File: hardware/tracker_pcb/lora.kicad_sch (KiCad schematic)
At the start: 3 parts, among them IC4 WIO-SX1262

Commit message: WIP
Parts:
- IC4: footprint 114993390 -> footprint:114993390
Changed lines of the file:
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@@
 			)
 		)
-		(property "Footprint" "114993390"
+		(property "Footprint" "footprint:114993390"
 			(at 139.7 166.04 0)
 			(effects

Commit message: Beef up 5v supply and add new power mux
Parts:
- renumbered C25 to C26, C24 to C27, IC4 to U12
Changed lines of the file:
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@@
 		(on_board yes)
 		(dnp no)
-		(property "Reference" "C24"
+		(property "Reference" "C27"
 			(at 92.202 92.964 0)
 			(effects
@@
 			(project "tracker_pcb"
 				(path "/6aaa9514-f94e-4843-90d0-16960e4e49cb/4b60d742-f193-431b-a1a9-b431b44dc8b4"
-					(reference "C24")
+					(reference "C27")
 					(unit 1)
 				)
@@
 		(on_board yes)
 		(dnp yes)
-		(property "Reference" "C25"
+		(property "Reference" "C26"
 			(at 78.232 92.964 0)
 			(effects
@@
 			(project "tracker_pcb"
 				(path "/6aaa9514-f94e-4843-90d0-16960e4e49cb/4b60d742-f193-431b-a1a9-b431b44dc8b4"
-					(reference "C25")
+					(reference "C26")
 					(unit 1)
 				)
@@
 		(dnp no)
 		(fields_autoplaced yes)
-		(property "Reference" "#PWR022"
+		(property "Reference" "#PWR026"
 			(at 127 105.41 0)
 			(effects
@@
 			(project ""
 				(path "/6aaa9514-f94e-4843-90d0-16960e4e49cb/4b60d742-f193-431b-a1a9-b431b44dc8b4"
-					(reference "#PWR022")
+					(reference "#PWR026")
 					(unit 1)
 				)
@@
 		(dnp yes)
 		(fields_autoplaced yes)
-		(property "Reference" "IC4"
+		(property "Reference" "U12"
 			(at 127 63.5 0)
 			(effects
@@
 			(project ""
 				(path "/6aaa9514-f94e-4843-90d0-16960e4e49cb/4b60d742-f193-431b-a1a9-b431b44dc8b4"
-					(reference "IC4")
+					(reference "U12")
 					(unit 1)
 				)

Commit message: Modify iso circuit for best CTR
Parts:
- renumbered C26 to C25, C27 to C26
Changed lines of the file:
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@@
 		(on_board yes)
 		(dnp no)
-		(property "Reference" "C27"
+		(property "Reference" "C26"
 			(at 92.202 92.964 0)
 			(effects
@@
 			(project "tracker_pcb"
 				(path "/6aaa9514-f94e-4843-90d0-16960e4e49cb/4b60d742-f193-431b-a1a9-b431b44dc8b4"
-					(reference "C27")
+					(reference "C26")
 					(unit 1)
 				)
@@
 		(on_board yes)
 		(dnp yes)
-		(property "Reference" "C26"
+		(property "Reference" "C25"
 			(at 78.232 92.964 0)
 			(effects
@@
 			(project "tracker_pcb"
 				(path "/6aaa9514-f94e-4843-90d0-16960e4e49cb/4b60d742-f193-431b-a1a9-b431b44dc8b4"
-					(reference "C26")
+					(reference "C25")
 					(unit 1)
 				)

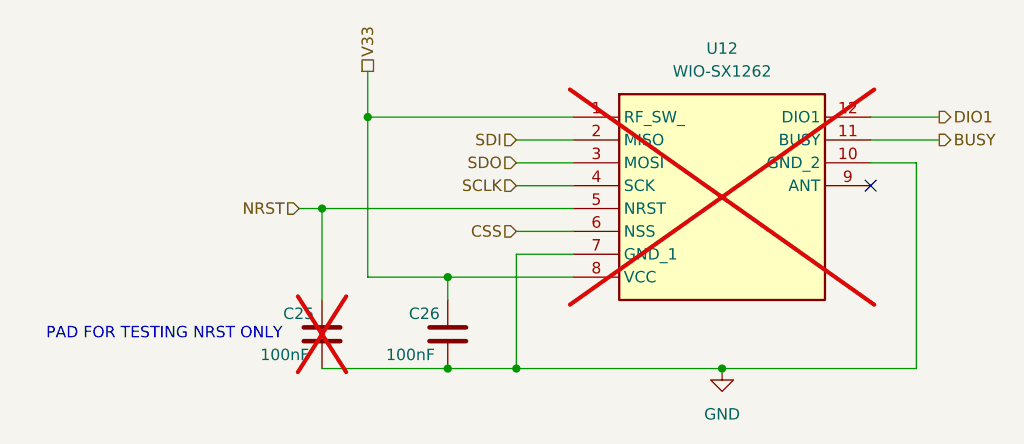
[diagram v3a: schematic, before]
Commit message: add 3pin jst for analog
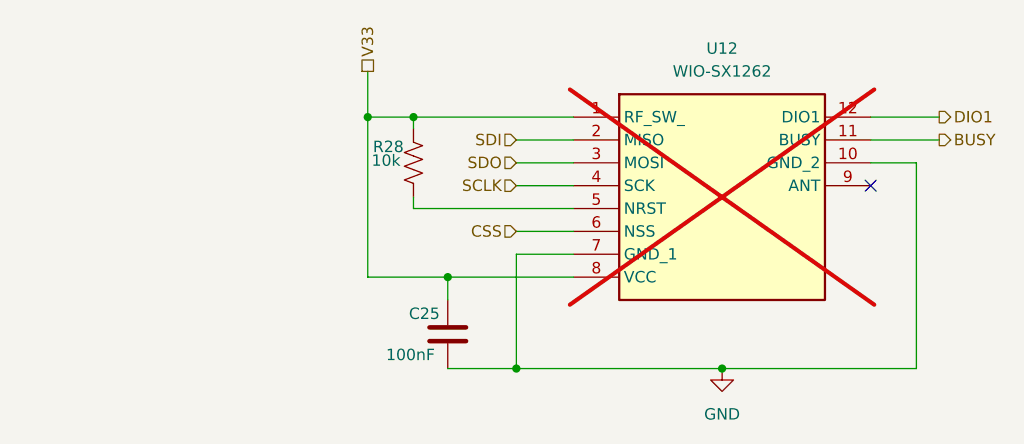
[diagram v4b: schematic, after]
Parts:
- removed C25: 100nF, Capacitor_SMD:C_0603_1608Metric, symbol Device:C
- added R28: 10k, Resistor_SMD:R_0805_2012Metric, symbol Device:R_US
- renumbered C26 to C25
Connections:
- net V33: now also R28.1
- net NRST: no longer names the net of U12.5 (NRST)
- net NRST: now also R28.2
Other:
- note removed: "PAD FOR TESTING NRST ONLY"

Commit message: v2 hardware changes
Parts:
- renumbered C25 to C27, R28 to R32, U12 to U13
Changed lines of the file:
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@@
 		(on_board yes)
 		(dnp no)
-		(property "Reference" "R28"
+		(property "Reference" "R32"
 			(at 89.916 74.422 0)
 			(effects
@@
 			(project "tracker_pcb"
 				(path "/6aaa9514-f94e-4843-90d0-16960e4e49cb/4b60d742-f193-431b-a1a9-b431b44dc8b4"
-					(reference "R28")
+					(reference "R32")
 					(unit 1)
 				)
@@
 		(on_board yes)
 		(dnp no)
-		(property "Reference" "C25"
+		(property "Reference" "C27"
 			(at 92.202 92.964 0)
 			(effects
@@
 			(project "tracker_pcb"
 				(path "/6aaa9514-f94e-4843-90d0-16960e4e49cb/4b60d742-f193-431b-a1a9-b431b44dc8b4"
-					(reference "C25")
+					(reference "C27")
 					(unit 1)
 				)
@@
 		(dnp no)
 		(fields_autoplaced yes)
-		(property "Reference" "#PWR026"
+		(property "Reference" "#PWR027"
 			(at 127 105.41 0)
 			(effects
@@
 			(project ""
 				(path "/6aaa9514-f94e-4843-90d0-16960e4e49cb/4b60d742-f193-431b-a1a9-b431b44dc8b4"
-					(reference "#PWR026")
+					(reference "#PWR027")
 					(unit 1)
 				)
@@
 		(dnp yes)
 		(fields_autoplaced yes)
-		(property "Reference" "U12"
+		(property "Reference" "U13"
 			(at 127 63.5 0)
 			(effects
@@
 			(project ""
 				(path "/6aaa9514-f94e-4843-90d0-16960e4e49cb/4b60d742-f193-431b-a1a9-b431b44dc8b4"
-					(reference "U12")
+					(reference "U13")
 					(unit 1)
 				)

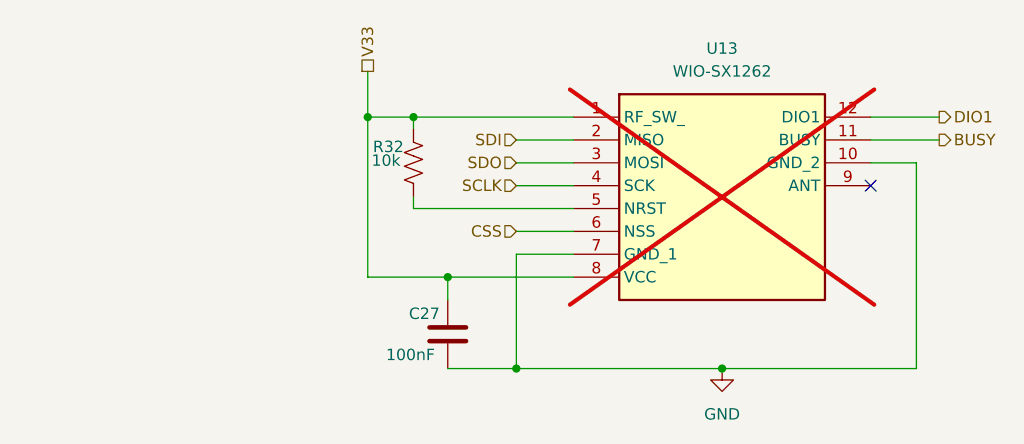
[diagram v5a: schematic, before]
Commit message: more motor safety
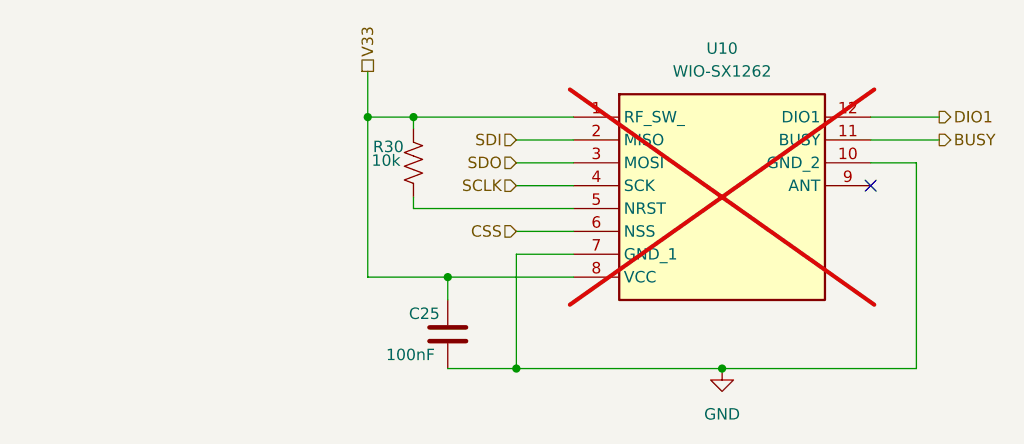
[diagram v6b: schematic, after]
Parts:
- renumbered C27 to C25, R32 to R30, U13 to U10
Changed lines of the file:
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@@
 		(on_board yes)
 		(dnp no)
-		(property "Reference" "R32"
+		(property "Reference" "R30"
 			(at 89.916 74.422 0)
 			(effects
@@
 			(project "tracker_pcb"
 				(path "/6aaa9514-f94e-4843-90d0-16960e4e49cb/4b60d742-f193-431b-a1a9-b431b44dc8b4"
-					(reference "R32")
+					(reference "R30")
 					(unit 1)
 				)
@@
 		(on_board yes)
 		(dnp no)
-		(property "Reference" "C27"
+		(property "Reference" "C25"
 			(at 92.202 92.964 0)
 			(effects
@@
 			(project "tracker_pcb"
 				(path "/6aaa9514-f94e-4843-90d0-16960e4e49cb/4b60d742-f193-431b-a1a9-b431b44dc8b4"
-					(reference "C27")
+					(reference "C25")
 					(unit 1)
 				)
@@
 		(dnp no)
 		(fields_autoplaced yes)
-		(property "Reference" "#PWR027"
+		(property "Reference" "#PWR024"
 			(at 127 105.41 0)
 			(effects
@@
 			(project ""
 				(path "/6aaa9514-f94e-4843-90d0-16960e4e49cb/4b60d742-f193-431b-a1a9-b431b44dc8b4"
-					(reference "#PWR027")
+					(reference "#PWR024")
 					(unit 1)
 				)
@@
 		(dnp yes)
 		(fields_autoplaced yes)
-		(property "Reference" "U13"
+		(property "Reference" "U10"
 			(at 127 63.5 0)
 			(effects
@@
 			(project ""
 				(path "/6aaa9514-f94e-4843-90d0-16960e4e49cb/4b60d742-f193-431b-a1a9-b431b44dc8b4"
-					(reference "U13")
+					(reference "U10")
 					(unit 1)
 				)
